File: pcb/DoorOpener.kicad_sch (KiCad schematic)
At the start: 7 parts, among them SW1 POWER, SW2 Button, U2 ESP-01v090

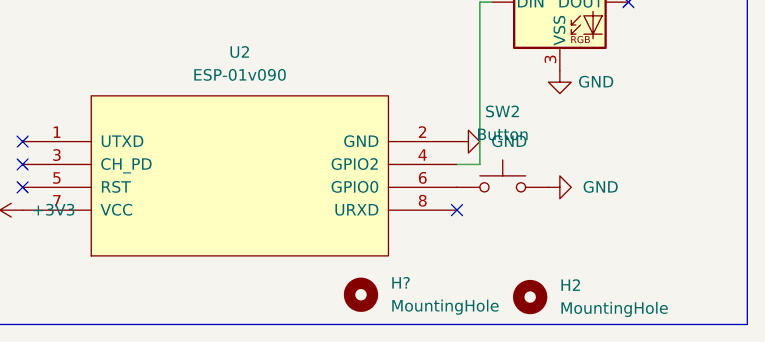
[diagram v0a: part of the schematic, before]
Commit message: Add mounting holes
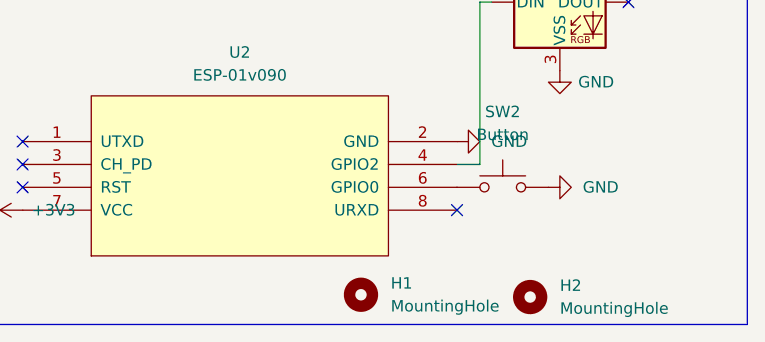
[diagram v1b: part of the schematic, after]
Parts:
- gave numbers to parts that had none: 1
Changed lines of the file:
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@@
   (symbol (lib_id "Mechanical:MountingHole") (at 150.622 108.204 0) (unit 1)
     (in_bom yes) (on_board yes) (fields_autoplaced)
-    (property "Reference" "H?" (id 0) (at 153.924 106.9339 0)
+    (property "Reference" "H1" (id 0) (at 153.924 106.9339 0)
       (effects (font (size 1.27 1.27)) (justify left))
     )
@@
       (reference "D1") (unit 1) (value "WS2812B") (footprint "LED_THT:LED_D5.0mm-4_RGB_Wide_Pins")
     )
+    (path "/9d8c40ac-1c2f-4145-8b2e-cf80bdb34b2b"
+      (reference "H1") (unit 1) (value "MountingHole") (footprint "MountingHole:MountingHole_3mm")
+    )
     (path "/a6152703-ca9a-41de-b3b5-08491c9de5bb"
       (reference "H2") (unit 1) (value "MountingHole") (footprint "MountingHole:MountingHole_3mm")
     )
-    (path "/9d8c40ac-1c2f-4145-8b2e-cf80bdb34b2b"
-      (reference "H?") (unit 1) (value "MountingHole") (footprint "MountingHole:MountingHole_3mm")
-    )
     (path "/a548b600-36d7-4fb4-bec6-833a61cb98e0"

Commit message: Prepare for milling the pcb
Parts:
- removed H2: MountingHole, MountingHole:MountingHole_3mm, symbol Mechanical:MountingHole
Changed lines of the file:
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@@
     (pin "8")
-  )
-  (symbol (lib_id "Mechanical:MountingHole") (at 169.418 108.458 0) (unit 1)
-    (in_bom yes) (on_board yes) (fields_autoplaced)
-    (property "Reference" "H2" (id 0) (at 172.72 107.1879 0)
-      (effects (font (size 1.27 1.27)) (justify left))
-    )
-    (property "Value" "MountingHole" (id 1) (at 172.72 109.7279 0)
-      (effects (font (size 1.27 1.27)) (justify left))
-    )
-    (property "Footprint" "MountingHole:MountingHole_3mm" (id 2) (at 169.418 108.458 0)
-      (effects (font (size 1.27 1.27)) hide)
-    )
-    (property "Datasheet" "~" (id 3) (at 169.418 108.458 0)
-      (effects (font (size 1.27 1.27)) hide)
-    )
   )
   (symbol (lib_id "power:+3V3") (at 172.72 68.072 0) (unit 1)
@@
       (reference "H1") (unit 1) (value "MountingHole") (footprint "MountingHole:MountingHole_3mm")
     )
-    (path "/a6152703-ca9a-41de-b3b5-08491c9de5bb"
-      (reference "H2") (unit 1) (value "MountingHole") (footprint "MountingHole:MountingHole_3mm")
-    )
     (path "/a548b600-36d7-4fb4-bec6-833a61cb98e0"

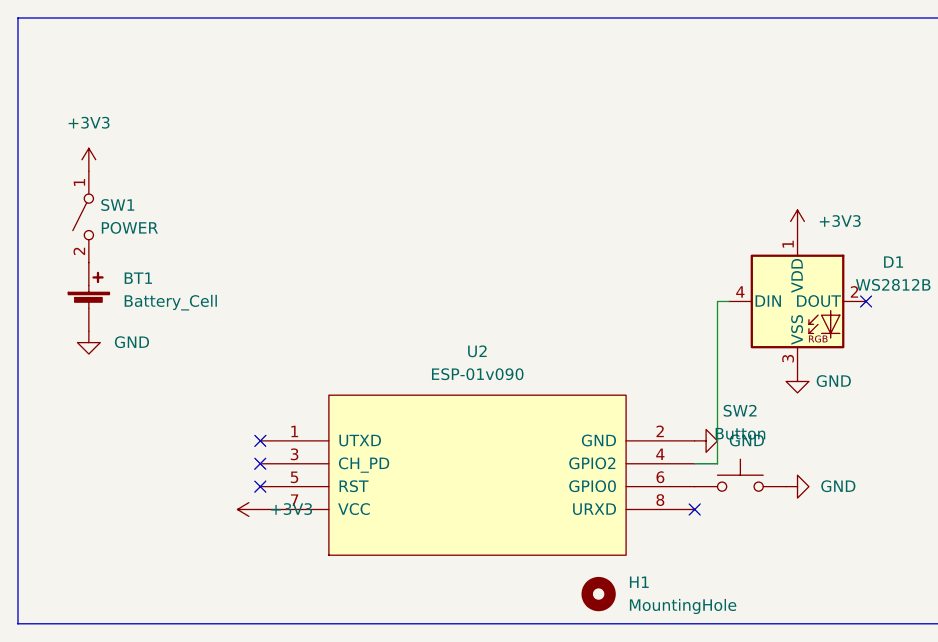
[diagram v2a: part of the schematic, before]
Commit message: Add TX RX Connector
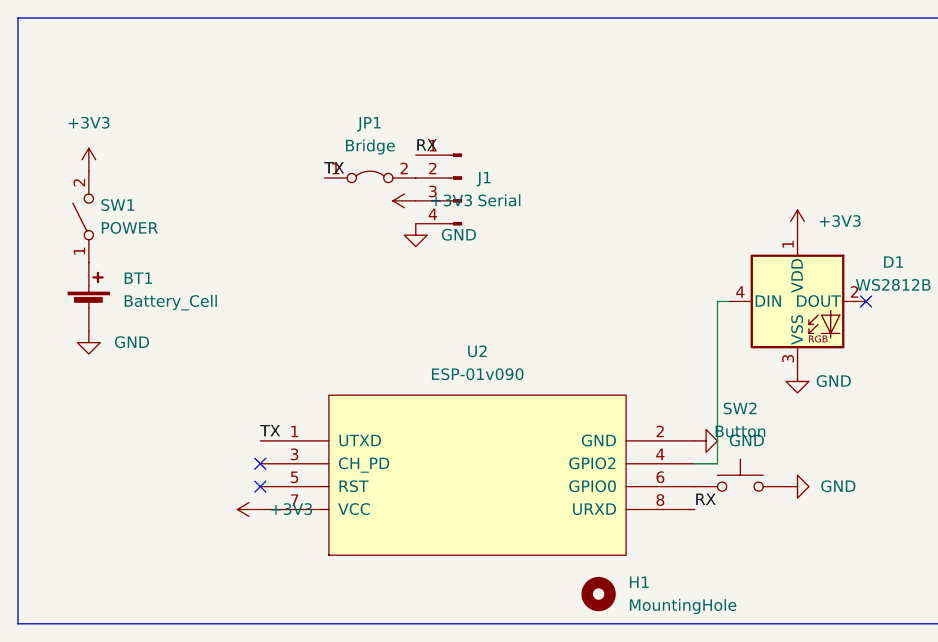
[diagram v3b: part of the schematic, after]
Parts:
- added J1: Serial, Connector_PinHeader_2.54mm:PinHeader_1x04_P2.54mm_Horizontal, symbol Connector:Conn_01x04_Male
- added JP1: Bridge, Resistor_THT:R_Axial_DIN0204_L3.6mm_D1.6mm_P5.08mm_Horizontal, symbol Jumper:Jumper_2_Bridged
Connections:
- net +3V3: now also SW1.2 (B), J1.3 (Pin_3); no longer SW1.1 (A)
- net GND: now also J1.4 (Pin_4)
- net at BT1.1 (+): now also SW1.1 (A); no longer SW1.2 (B)
- net TX: now reaches U2.1 (UTXD)
- net TX: now also JP1.1 (A)
- net RX: now reaches U2.8 (URXD)
- net RX: now also J1.1 (Pin_1)
- new net: J1.2 (Pin_2), JP1.2 (B)
- no-connect marks 5 -> 3
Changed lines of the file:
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@@
   (paper "A4")
   (no_connect (at 180.34 75.692))
-  (no_connect (at 113.03 91.186))
   (no_connect (at 113.03 93.726))
   (no_connect (at 113.03 96.266))
-  (no_connect (at 161.29 98.806))
   (polyline (pts (xy 86.106 111.506) (xy 86.106 44.196))
     (stroke (width 0) (type default) (color 0 0 0 0))
@@
     (stroke (width 0) (type default) (color 0 0 0 0))
   )
+  (label "RX" (at 161.29 98.806 0)
+    (effects (font (size 1.27 1.27)) (justify left bottom))
+  )
+  (label "TX" (at 120.142 61.976 0)
+    (effects (font (size 1.27 1.27)) (justify left bottom))
+  )
+  (label "RX" (at 130.302 59.436 0)
+    (effects (font (size 1.27 1.27)) (justify left bottom))
+  )
+  (label "TX" (at 113.03 91.186 0)
+    (effects (font (size 1.27 1.27)) (justify left bottom))
+  )
   (symbol (lib_id "power:GND") (at 171.45 96.266 90) (unit 1)
     (in_bom yes) (on_board yes) (fields_autoplaced)
@@
     (pin "1")
   )
+  (symbol (lib_id "power:GND") (at 130.302 67.056 0) (unit 1)
+    (in_bom yes) (on_board yes) (fields_autoplaced)
+    (property "Reference" "#PWR0108" (id 0) (at 130.302 73.406 0)
+      (effects (font (size 1.27 1.27)) hide)
+    )
+    (property "Value" "GND" (id 1) (at 133.096 68.3259 0)
+      (effects (font (size 1.27 1.27)) (justify left))
+    )
+    (property "Footprint" "" (id 2) (at 130.302 67.056 0)
+      (effects (font (size 1.27 1.27)) hide)
+    )
+    (property "Datasheet" "" (id 3) (at 130.302 67.056 0)
+      (effects (font (size 1.27 1.27)) hide)
+    )
+    (pin "1")
+  )
   (symbol (lib_id "power:GND") (at 93.98 78.994 0) (unit 1)
     (in_bom yes) (on_board yes) (fields_autoplaced)
@@
     )
     (pin "1")
+  )
+  (symbol (lib_id "Jumper:Jumper_2_Bridged") (at 125.222 61.976 0) (unit 1)
+    (in_bom yes) (on_board yes) (fields_autoplaced)
+    (property "Reference" "JP1" (id 0) (at 125.222 55.88 0))
+    (property "Value" "Bridge" (id 1) (at 125.222 58.42 0))
+    (property "Footprint" "Resistor_THT:R_Axial_DIN0204_L3.6mm_D1.6mm_P5.08mm_Horizontal" (id 2) (at 125.222 61.976 0)
+      (effects (font (size 1.27 1.27)) hide)
+    )
+    (property "Datasheet" "~" (id 3) (at 125.222 61.976 0)
+      (effects (font (size 1.27 1.27)) hide)
+    )
+    (pin "1")
+    (pin "2")
   )
   (symbol (lib_id "power:+3V3") (at 93.98 61.214 0) (unit 1)
@@
   (symbol (lib_id "Switch:SW_Push") (at 166.37 96.266 0) (unit 1)
     (in_bom yes) (on_board yes) (fields_autoplaced)
-    (property "Reference" "SW2" (id 0) (at 166.37 87.884 0))
-    (property "Value" "Button" (id 1) (at 166.37 90.424 0))
+    (property "Reference" "SW2" (id 0) (at 166.37 87.63 0))
+    (property "Value" "Button" (id 1) (at 166.37 90.17 0))
     (property "Footprint" "Button_Switch_THT:SW_PUSH_6mm_H4.3mm" (id 2) (at 166.37 91.186 0)
       (effects (font (size 1.27 1.27)) hide)
@@
     (pin "2")
   )
-  (symbol (lib_id "Switch:SW_SPST") (at 93.98 66.294 90) (mirror x) (unit 1)
+  (symbol (lib_id "Switch:SW_SPST") (at 93.98 66.294 90) (unit 1)
     (in_bom yes) (on_board yes) (fields_autoplaced)
     (property "Reference" "SW1" (id 0) (at 95.25 65.0239 90)
@@
     (pin "1")
   )
+  (symbol (lib_id "Connector:Conn_01x04_Male") (at 135.382 61.976 0) (mirror y) (unit 1)
+    (in_bom yes) (on_board yes) (fields_autoplaced)
+    (property "Reference" "J1" (id 0) (at 137.16 61.9759 0)
+      (effects (font (size 1.27 1.27)) (justify right))
+    )
+    (property "Value" "Serial" (id 1) (at 137.16 64.5159 0)
+      (effects (font (size 1.27 1.27)) (justify right))
+    )
+    (property "Footprint" "Connector_PinHeader_2.54mm:PinHeader_1x04_P2.54mm_Horizontal" (id 2) (at 135.382 61.976 0)
+      (effects (font (size 1.27 1.27)) hide)
+    )
+    (property "Datasheet" "~" (id 3) (at 135.382 61.976 0)
+      (effects (font (size 1.27 1.27)) hide)
+    )
+    (pin "1")
+    (pin "2")
+    (pin "3")
+    (pin "4")
+  )
+  (symbol (lib_id "power:+3V3") (at 130.302 64.516 90) (unit 1)
+    (in_bom yes) (on_board yes) (fields_autoplaced)
+    (property "Reference" "#PWR0109" (id 0) (at 134.112 64.516 0)
+      (effects (font (size 1.27 1.27)) hide)
+    )
+    (property "Value" "+3V3" (id 1) (at 131.826 64.5159 90)
+      (effects (font (size 1.27 1.27)) (justify right))
+    )
+    (property "Footprint" "" (id 2) (at 130.302 64.516 0)
+      (effects (font (size 1.27 1.27)) hide)
+    )
+    (property "Datasheet" "" (id 3) (at 130.302 64.516 0)
+      (effects (font (size 1.27 1.27)) hide)
+    )
+    (pin "1")
+  )
   (sheet_instances
     (path "/" (page "1"))
@@
       (reference "#PWR0107") (unit 1) (value "GND") (footprint "")
     )
+    (path "/24e2ce02-6f31-4273-8910-6adaf32d3514"
+      (reference "#PWR0108") (unit 1) (value "GND") (footprint "")
+    )
+    (path "/e197fbf2-e7da-43c3-8555-1fd25cf6bbd7"
+      (reference "#PWR0109") (unit 1) (value "+3V3") (footprint "")
+    )
     (path "/d607acbe-2303-4604-aeda-edef70e2d201"
       (reference "BT1") (unit 1) (value "Battery_Cell") (footprint "Battery:BatteryHolder_Keystone_2479_3xAAA")
@@
       (reference "H1") (unit 1) (value "MountingHole") (footprint "MountingHole:MountingHole_3mm")
     )
+    (path "/da14771c-1849-4752-a0aa-20a08dec5ac4"
+      (reference "J1") (unit 1) (value "Serial") (footprint "Connector_PinHeader_2.54mm:PinHeader_1x04_P2.54mm_Horizontal")
+    )
+    (path "/37204591-45c3-440b-a507-d0392365311c"
+      (reference "JP1") (unit 1) (value "Bridge") (footprint "Resistor_THT:R_Axial_DIN0204_L3.6mm_D1.6mm_P5.08mm_Horizontal")
+    )
     (path "/a548b600-36d7-4fb4-bec6-833a61cb98e0"

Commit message: Version 0.2
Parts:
- removed H1: MountingHole, MountingHole:MountingHole_3mm, symbol Mechanical:MountingHole
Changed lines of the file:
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@@
     (pin "1")
-  )
-  (symbol (lib_id "Mechanical:MountingHole") (at 150.622 108.204 0) (unit 1)
-    (in_bom yes) (on_board yes) (fields_autoplaced)
-    (property "Reference" "H1" (id 0) (at 153.924 106.9339 0)
-      (effects (font (size 1.27 1.27)) (justify left))
-    )
-    (property "Value" "MountingHole" (id 1) (at 153.924 109.4739 0)
-      (effects (font (size 1.27 1.27)) (justify left))
-    )
-    (property "Footprint" "MountingHole:MountingHole_3mm" (id 2) (at 150.622 108.204 0)
-      (effects (font (size 1.27 1.27)) hide)
-    )
-    (property "Datasheet" "~" (id 3) (at 150.622 108.204 0)
-      (effects (font (size 1.27 1.27)) hide)
-    )
   )
   (symbol (lib_id "Switch:SW_Push") (at 166.37 96.266 0) (unit 1)
@@
       (reference "D1") (unit 1) (value "WS2812B") (footprint "LED_THT:LED_D5.0mm-4_RGB_Wide_Pins")
     )
-    (path "/9d8c40ac-1c2f-4145-8b2e-cf80bdb34b2b"
-      (reference "H1") (unit 1) (value "MountingHole") (footprint "MountingHole:MountingHole_3mm")
-    )
     (path "/da14771c-1849-4752-a0aa-20a08dec5ac4"

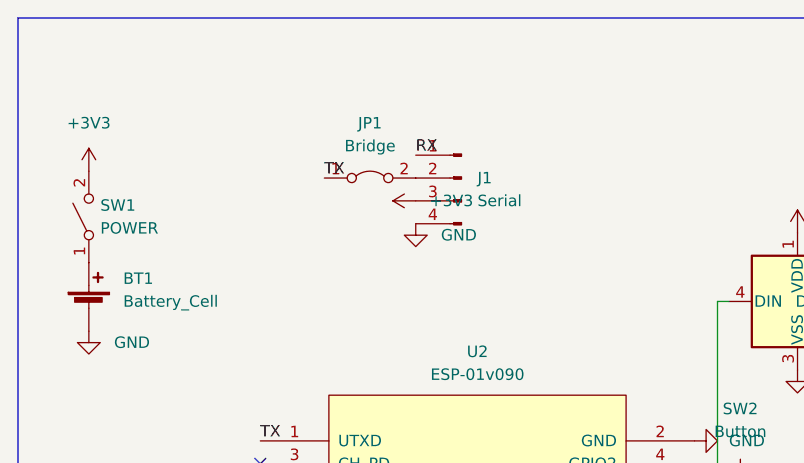
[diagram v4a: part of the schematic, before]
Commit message: Add FTDI-compatible socket and an option to power from USB
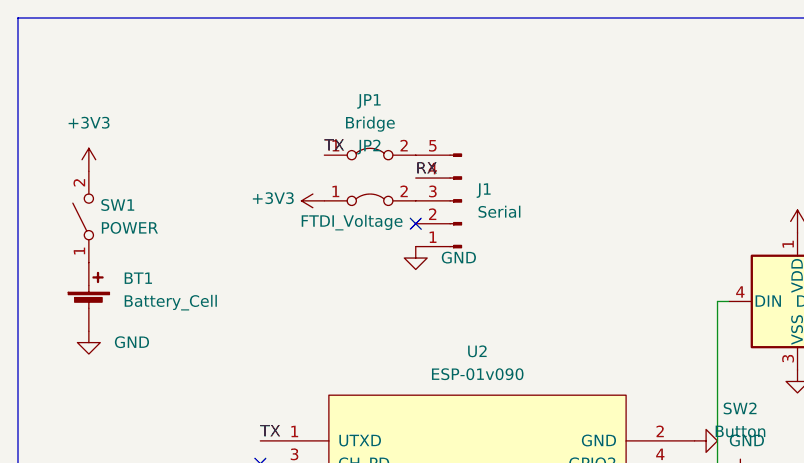
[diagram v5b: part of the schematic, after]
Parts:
- removed J1: Serial, Connector_PinHeader_2.54mm:PinHeader_1x04_P2.54mm_Horizontal, symbol Connector:Conn_01x04_Male
- added J1: Serial, Connector_PinHeader_2.54mm:PinHeader_1x05_P2.54mm_Horizontal, symbol Connector:Conn_01x05_Male
- added JP2: FTDI_Voltage, Connector_PinHeader_2.54mm:PinHeader_1x02_P2.54mm_Vertical, symbol Jumper:Jumper_2_Bridged
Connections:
- net +3V3: now also JP2.1 (A)
- net GND: now also J1.1 (Pin_1)
- net RX: now also J1.4 (Pin_4)
- net at JP1.2 (B): now also J1.5 (Pin_5)
- new net: J1.3 (Pin_3), JP2.2 (B)
- no-connect marks 3 -> 4
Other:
- moved on the sheet: JP1
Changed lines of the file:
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@@
   (no_connect (at 113.03 93.726))
   (no_connect (at 113.03 96.266))
+  (no_connect (at 130.302 67.056))
   (polyline (pts (xy 86.106 111.506) (xy 86.106 44.196))
     (stroke (width 0) (type default) (color 0 0 0 0))
@@
     (effects (font (size 1.27 1.27)) (justify left bottom))
   )
-  (label "TX" (at 120.142 61.976 0)
+  (label "TX" (at 120.142 59.436 0)
     (effects (font (size 1.27 1.27)) (justify left bottom))
   )
-  (label "RX" (at 130.302 59.436 0)
+  (label "RX" (at 130.302 61.976 0)
     (effects (font (size 1.27 1.27)) (justify left bottom))
   )
@@
     (effects (font (size 1.27 1.27)) (justify left bottom))
   )
+  (symbol (lib_id "power:+3V3") (at 120.142 64.516 90) (unit 1)
+    (in_bom yes) (on_board yes)
+    (property "Reference" "#PWR0109" (id 0) (at 123.952 64.516 0)
+      (effects (font (size 1.27 1.27)) hide)
+    )
+    (property "Value" "+3V3" (id 1) (at 112.014 64.262 90)
+      (effects (font (size 1.27 1.27)) (justify right))
+    )
+    (property "Footprint" "" (id 2) (at 120.142 64.516 0)
+      (effects (font (size 1.27 1.27)) hide)
+    )
+    (property "Datasheet" "" (id 3) (at 120.142 64.516 0)
+      (effects (font (size 1.27 1.27)) hide)
+    )
+    (pin "1")
+  )
   (symbol (lib_id "power:GND") (at 171.45 96.266 90) (unit 1)
     (in_bom yes) (on_board yes) (fields_autoplaced)
@@
     (pin "1")
   )
-  (symbol (lib_id "power:GND") (at 130.302 67.056 0) (unit 1)
-    (in_bom yes) (on_board yes) (fields_autoplaced)
-    (property "Reference" "#PWR0108" (id 0) (at 130.302 73.406 0)
-      (effects (font (size 1.27 1.27)) hide)
-    )
-    (property "Value" "GND" (id 1) (at 133.096 68.3259 0)
-      (effects (font (size 1.27 1.27)) (justify left))
-    )
-    (property "Footprint" "" (id 2) (at 130.302 67.056 0)
-      (effects (font (size 1.27 1.27)) hide)
-    )
-    (property "Datasheet" "" (id 3) (at 130.302 67.056 0)
+  (symbol (lib_id "power:GND") (at 130.302 69.596 0) (unit 1)
+    (in_bom yes) (on_board yes) (fields_autoplaced)
+    (property "Reference" "#PWR0108" (id 0) (at 130.302 75.946 0)
+      (effects (font (size 1.27 1.27)) hide)
+    )
+    (property "Value" "GND" (id 1) (at 133.096 70.8659 0)
+      (effects (font (size 1.27 1.27)) (justify left))
+    )
+    (property "Footprint" "" (id 2) (at 130.302 69.596 0)
+      (effects (font (size 1.27 1.27)) hide)
+    )
+    (property "Datasheet" "" (id 3) (at 130.302 69.596 0)
       (effects (font (size 1.27 1.27)) hide)
     )
@@
     (pin "1")
   )
-  (symbol (lib_id "Jumper:Jumper_2_Bridged") (at 125.222 61.976 0) (unit 1)
-    (in_bom yes) (on_board yes) (fields_autoplaced)
-    (property "Reference" "JP1" (id 0) (at 125.222 55.88 0))
-    (property "Value" "Bridge" (id 1) (at 125.222 58.42 0))
-    (property "Footprint" "Resistor_THT:R_Axial_DIN0204_L3.6mm_D1.6mm_P5.08mm_Horizontal" (id 2) (at 125.222 61.976 0)
-      (effects (font (size 1.27 1.27)) hide)
-    )
-    (property "Datasheet" "~" (id 3) (at 125.222 61.976 0)
+  (symbol (lib_id "Jumper:Jumper_2_Bridged") (at 125.222 59.436 0) (unit 1)
+    (in_bom yes) (on_board yes) (fields_autoplaced)
+    (property "Reference" "JP1" (id 0) (at 125.222 53.34 0))
+    (property "Value" "Bridge" (id 1) (at 125.222 55.88 0))
+    (property "Footprint" "Resistor_THT:R_Axial_DIN0204_L3.6mm_D1.6mm_P5.08mm_Horizontal" (id 2) (at 125.222 59.436 0)
+      (effects (font (size 1.27 1.27)) hide)
+    )
+    (property "Datasheet" "~" (id 3) (at 125.222 59.436 0)
       (effects (font (size 1.27 1.27)) hide)
     )
@@
     (pin "3")
     (pin "4")
+  )
+  (symbol (lib_id "Jumper:Jumper_2_Bridged") (at 125.222 64.516 0) (unit 1)
+    (in_bom yes) (on_board yes)
+    (property "Reference" "JP2" (id 0) (at 125.222 58.42 0))
+    (property "Value" "FTDI_Voltage" (id 1) (at 123.19 66.802 0))
+    (property "Footprint" "Connector_PinHeader_2.54mm:PinHeader_1x02_P2.54mm_Vertical" (id 2) (at 125.222 64.516 0)
+      (effects (font (size 1.27 1.27)) hide)
+    )
+    (property "Datasheet" "~" (id 3) (at 125.222 64.516 0)
+      (effects (font (size 1.27 1.27)) hide)
+    )
+    (pin "1")
+    (pin "2")
   )
   (symbol (lib_id "power:+3V3") (at 113.03 98.806 90) (unit 1)
@@
     (pin "1")
   )
-  (symbol (lib_id "Connector:Conn_01x04_Male") (at 135.382 61.976 0) (mirror y) (unit 1)
-    (in_bom yes) (on_board yes) (fields_autoplaced)
-    (property "Reference" "J1" (id 0) (at 137.16 61.9759 0)
-      (effects (font (size 1.27 1.27)) (justify right))
-    )
-    (property "Value" "Serial" (id 1) (at 137.16 64.5159 0)
-      (effects (font (size 1.27 1.27)) (justify right))
-    )
-    (property "Footprint" "Connector_PinHeader_2.54mm:PinHeader_1x04_P2.54mm_Horizontal" (id 2) (at 135.382 61.976 0)
-      (effects (font (size 1.27 1.27)) hide)
-    )
-    (property "Datasheet" "~" (id 3) (at 135.382 61.976 0)
+  (symbol (lib_id "Connector:Conn_01x05_Male") (at 135.382 64.516 180) (unit 1)
+    (in_bom yes) (on_board yes) (fields_autoplaced)
+    (property "Reference" "J1" (id 0) (at 137.16 63.2459 0)
+      (effects (font (size 1.27 1.27)) (justify right))
+    )
+    (property "Value" "Serial" (id 1) (at 137.16 65.7859 0)
+      (effects (font (size 1.27 1.27)) (justify right))
+    )
+    (property "Footprint" "Connector_PinHeader_2.54mm:PinHeader_1x05_P2.54mm_Horizontal" (id 2) (at 135.382 64.516 0)
+      (effects (font (size 1.27 1.27)) hide)
+    )
+    (property "Datasheet" "~" (id 3) (at 135.382 64.516 0)
       (effects (font (size 1.27 1.27)) hide)
     )
@@
     (pin "3")
     (pin "4")
-  )
-  (symbol (lib_id "power:+3V3") (at 130.302 64.516 90) (unit 1)
-    (in_bom yes) (on_board yes) (fields_autoplaced)
-    (property "Reference" "#PWR0109" (id 0) (at 134.112 64.516 0)
-      (effects (font (size 1.27 1.27)) hide)
-    )
-    (property "Value" "+3V3" (id 1) (at 131.826 64.5159 90)
-      (effects (font (size 1.27 1.27)) (justify right))
-    )
-    (property "Footprint" "" (id 2) (at 130.302 64.516 0)
-      (effects (font (size 1.27 1.27)) hide)
-    )
-    (property "Datasheet" "" (id 3) (at 130.302 64.516 0)
-      (effects (font (size 1.27 1.27)) hide)
-    )
-    (pin "1")
+    (pin "5")
   )
   (sheet_instances
@@
       (reference "#PWR0108") (unit 1) (value "GND") (footprint "")
     )
-    (path "/e197fbf2-e7da-43c3-8555-1fd25cf6bbd7"
+    (path "/16da7773-ee53-419b-a262-f0dc202cbf93"
       (reference "#PWR0109") (unit 1) (value "+3V3") (footprint "")
     )
@@
       (reference "D1") (unit 1) (value "WS2812B") (footprint "LED_THT:LED_D5.0mm-4_RGB_Wide_Pins")
     )
-    (path "/da14771c-1849-4752-a0aa-20a08dec5ac4"
-      (reference "J1") (unit 1) (value "Serial") (footprint "Connector_PinHeader_2.54mm:PinHeader_1x04_P2.54mm_Horizontal")
+    (path "/ea5902ef-573d-4f6d-a4b4-600ada26bc09"
+      (reference "J1") (unit 1) (value "Serial") (footprint "Connector_PinHeader_2.54mm:PinHeader_1x05_P2.54mm_Horizontal")
     )
     (path "/37204591-45c3-440b-a507-d0392365311c"
       (reference "JP1") (unit 1) (value "Bridge") (footprint "Resistor_THT:R_Axial_DIN0204_L3.6mm_D1.6mm_P5.08mm_Horizontal")
     )
+    (path "/90a95518-bfac-43e6-b071-a2d2bd99cec4"
+      (reference "JP2") (unit 1) (value "FTDI_Voltage") (footprint "Connector_PinHeader_2.54mm:PinHeader_1x02_P2.54mm_Vertical")
+    )
     (path "/a548b600-36d7-4fb4-bec6-833a61cb98e0"
